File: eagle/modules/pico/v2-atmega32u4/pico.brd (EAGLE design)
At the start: 93.3 x 53.3 mm, 45 parts, among them IC1 MEGA8-AI, IC3 ULN2803A, IC4 ULN2803A, J1 RS232, X1 16MHz

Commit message: Update atmega32u4
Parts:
- added C8: 10u, rcl:SMC_B
- added C9: 100n, SmartPrj:C0603-ROUND
- added F3: MF-MSMF050-2 500mA, rcl:L1812
- added J2: USB MICRO, SmartPrj:CON2_USB_MICRO_B_AT
- added L2: MH2029-300Y, wuerth-elektronik:0805
- added RN3: 22R, resistor-dil:CAY16
- added U1: ATMEGA32U4-XUMU, SmartPrj:QFN44ML7X7
- added Z1, Z2: CG0603MLC-05E, varistor:CT/CN0603
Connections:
- removed net N$4: C1.2, IC1.20
- new net A4: U1.40
- new net A5: U1.41
- new net AVCC: IC1.18
- new net D+: J2.P3, RN3.8, Z1.1
- new net D-: J2.P2, RN3.5, Z2.1
- new net D5*: U1.31
- new net D6*: U1.27
- new net HWB: U1.33
- new net IO10*: U1.30
- new net IO11*: U1.12
- new net IO12: U1.26
- new net IO13*: U1.32
- new net IO8: U1.28
- new net IO9*: U1.29
- new net N$10: C1.2, U1.24, U1.44
- new net N$11: IC1.4, IC1.6
- new net N$12: IC1.3, IC1.5
- new net PAD: U1.EXP
- new net RD+: RN3.1, U1.4
- new net RD-: RN3.4, U1.3
- new net RXLED: U1.8
- new net TXLED: U1.22
- new net UGND: J2.P5, L2.1, U1.5
- new net USBID: J2.P4
- new net UVCC: U1.2
- new net VUSB: C8.+, C9.2, F3.1
- new net XUSB: F3.2, J2.P1
- net 5V: now also U1.14, U1.34, U1.42; no longer IC1.18, IC1.4, IC1.6
- net A0: now also U1.36
- net A1: now also U1.37
- net A2: now also U1.38
- net A3: now also U1.39
- net D14: now also U1.16; no longer IC1.7
- net D15: now also U1.17; no longer IC1.8
- net D4: now also U1.25
- net D7: now also U1.1
- net GND: now also C8.-, C9.1, J2.S1, J2.S2, J2.S3, J2.S4, J2.S5, J2.S6, L2.2, U1.15, U1.23, U1.35, U1.43, Z1.2, Z2.2; no longer IC1.3, IC1.5
- net MISO: now also U1.11; no longer IC1.16
- net MOSI: now also U1.10; no longer IC1.15
- net RESET: now also U1.13; no longer IC1.29
- net RX: now also U1.20; no longer IC1.30
- net SCK: now also U1.9; no longer IC1.17
- net SCL: now also U1.18
- net SDA: now also U1.19; no longer IC1.27
- net TX: now also U1.21; no longer IC1.31

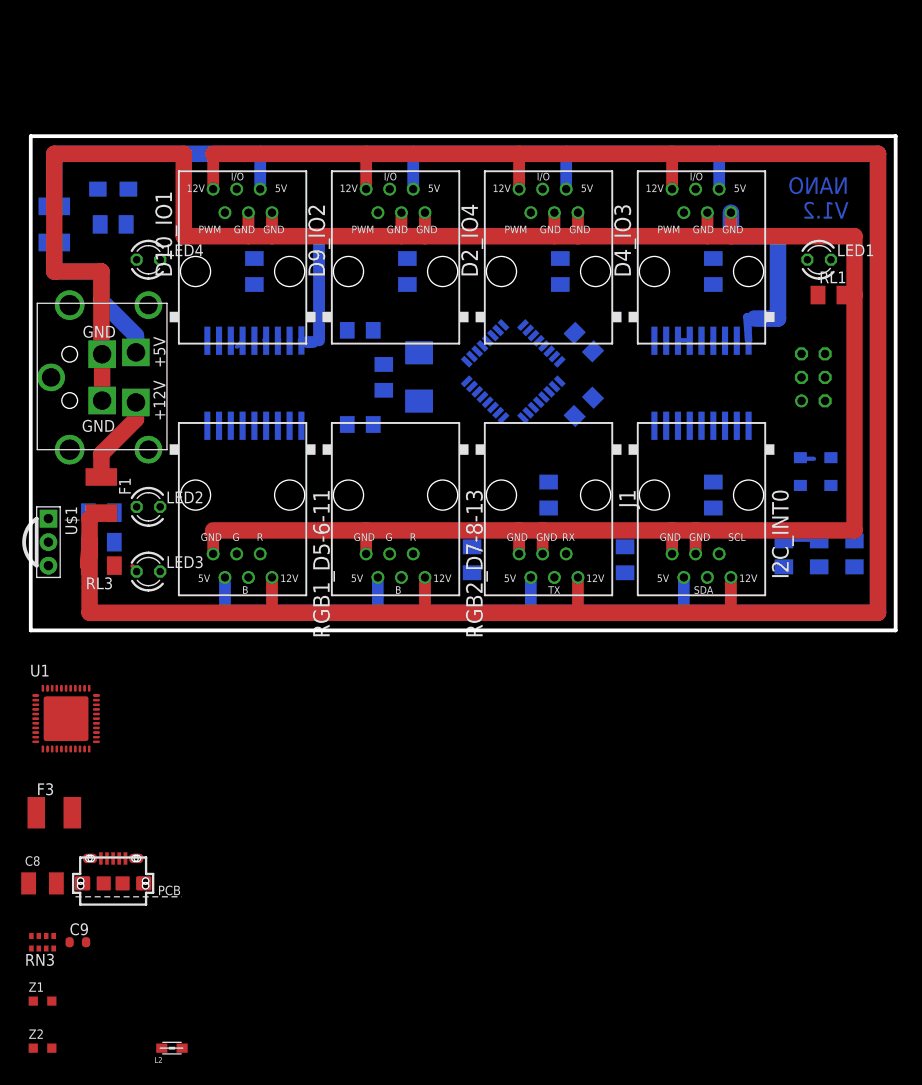
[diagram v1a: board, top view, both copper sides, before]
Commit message: Update library and atmega32u4
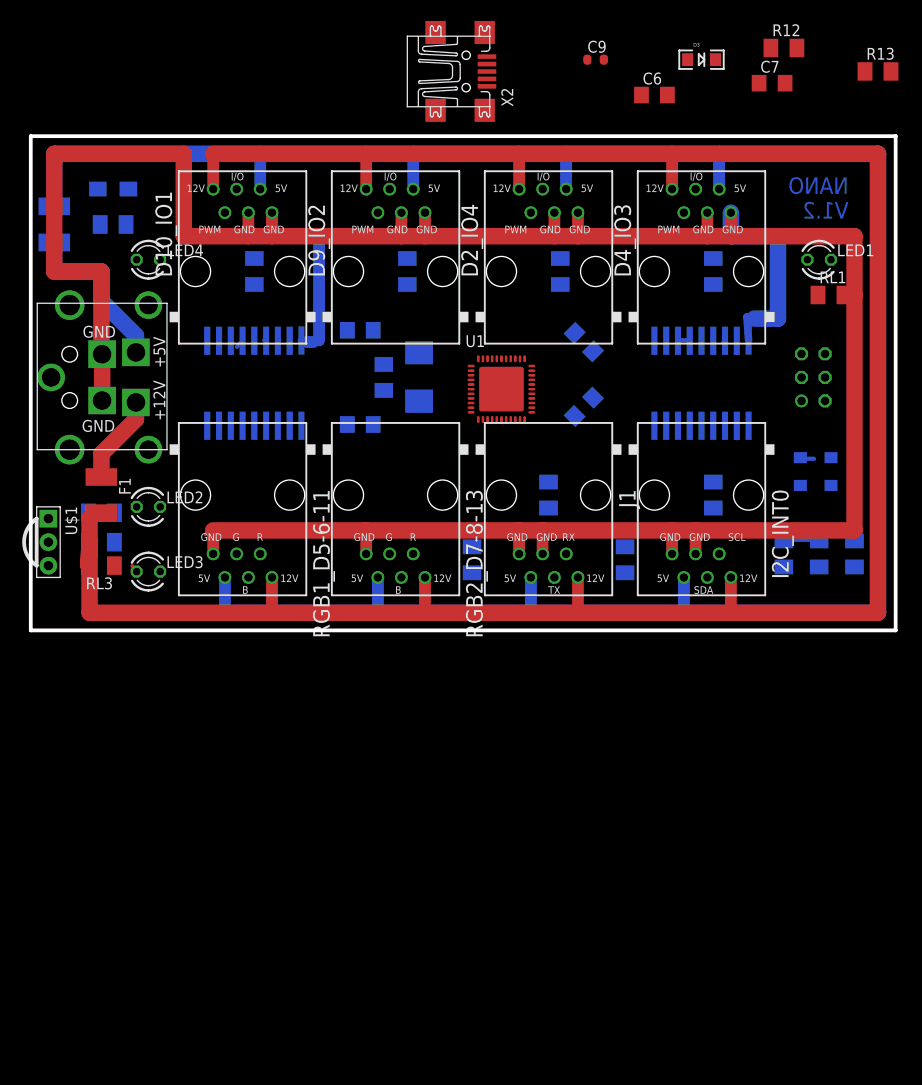
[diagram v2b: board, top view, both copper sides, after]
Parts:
- removed C8: 10u, rcl:SMC_B
- removed F3: MF-MSMF050-2 500mA, rcl:L1812
- removed IC1: MEGA8-AI, atmel:TQFP32-08
- removed J2: USB MICRO, SmartPrj:CON2_USB_MICRO_B_AT
- removed L2: MH2029-300Y, wuerth-elektronik:0805
- removed RN3: 22R, resistor-dil:CAY16
- removed Z1, Z2: CG0603MLC-05E, varistor:CT/CN0603
- added C6: 1uF, resistor:C1206
- added C7: 10uF, resistor:C1206
- added D3: 1N581D1206, lpatiny:LED-1206
- added R12, R13: 22, resistor:M1206
- added X2: MINI-USB-UX60-MB-5ST, con-hirose:UX60-MB-5ST
- moved C9 110.4 mm to (61.0, 61.0)
- moved U1 58.9 mm to (50.8, 25.4)
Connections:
- net IO12 renamed D12
- removed net A0: IC1.23, R0.2, U1.36
- removed net A1: IC1.24, R1B.2, U1.37
- removed net A2: IC1.25, R4.2, U1.38
- removed net A3: IC1.26, R9.2, U1.39
- removed net A4: U1.40
- removed net A5: U1.41
- removed net A6: IC1.19
- removed net A7: IC1.22
- removed net AVCC: IC1.18
- removed net D2: IC1.32, IC3.5
- removed net D3: IC1.1, R11.2
- removed net D5*: U1.31
- removed net D6*: U1.27
- removed net IO10*: U1.30
- removed net IO11*: U1.12
- removed net IO13*: U1.32
- removed net IO8: U1.28
- removed net IO9*: U1.29
- removed net N$11: IC1.4, IC1.6
- removed net N$12: IC1.3, IC1.5
- removed net UGND: J2.P5, L2.1, U1.5
- removed net USBID: J2.P4
- removed net UVCC: U1.2
- removed net XUSB: F3.2, J2.P1
- new net D11: IC3.7, U1.12
- new net D13: IC3.5, U1.32
- new net D18: R4.2, U1.36
- new net D19: R1B.2, U1.37
- new net D20: R0.2, U1.38
- new net D21: IC4.7, IC4.8, R11.2, U1.39
- new net D22: IC3.1, IC3.2, U1.40
- new net D23: IC3.3, IC3.4, U1.41
- new net N$4: C6.1, U1.6
- net 5V: now also C9.2, D3.C, U1.2
- net D+: now also R12.2, X2.3; no longer J2.P3, RN3.8, Z1.1
- net D-: now also R13.2, X2.2; no longer J2.P2, RN3.5, Z2.1
- net D10: now also IC4.5, IC4.6, U1.30; no longer IC1.14, IC3.8
- net D4: now also IC3.8; no longer IC1.2, IC3.6
- net D5: now also U1.31; no longer IC1.9
- net D6: now also IC3.6, U1.27; no longer IC1.10, IC4.3, IC4.4
- net D7: no longer IC1.11, IC4.7, IC4.8
- net D8: now also R9.2, U1.28; no longer IC1.12, IC3.1, IC3.2
- net D9: now also IC4.3, IC4.4, U1.29; no longer IC1.13, IC3.7
- net GND: now also C6.2, C7.1, U1.5, X2.5; no longer C8.-, IC1.21, J2.S1, J2.S2, J2.S3, J2.S4, J2.S5, J2.S6, L2.2, Z1.2, Z2.2
- net MOSI: no longer IC4.5, IC4.6
- net RD+: now also R12.1; no longer RN3.1
- net RD-: now also R13.1; no longer RN3.4
- net SCK: no longer IC3.3, IC3.4
- net SCL: no longer IC1.28
- net VUSB: now also C7.2, D3.A, U1.7, X2.1; no longer C8.+, C9.2, F3.1
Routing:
- net SCK: track 1.36 -> 0.00 mm
- net D23: track 0.00 -> 1.36 mm
- net D6: track 1.10 -> 0.17 mm
- net D9: track 0.21 -> 1.10 mm

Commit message: Update atmega32u8
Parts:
- added LED5: BICOLOR-LED, lpatiny:BICOLOR-3MM
- added RL5, RL6: 1K, resistor:M1206
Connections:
- new net N$11: LED5.3, RL5.2
- new net N$12: LED5.1, RL6.2
- net GND: now also LED5.2
- net RXLED: now also RL5.1
- net TXLED: now also RL6.1
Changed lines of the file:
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@@
 <element name="C6" library="resistor" package="C1206" value="1uF" x="67.31" y="57.15"/>
 <element name="C7" library="resistor" package="C1206" value="10uF" x="80.01" y="58.42"/>
+<element name="LED5" library="lpatiny" package="BICOLOR-3MM" value="BICOLOR-LED" x="2.54" y="-8.89"/>
+<element name="RL5" library="resistor" package="M1206" value="1K" x="2.54" y="-15.24"/>
+<element name="RL6" library="resistor" package="M1206" value="1K" x="2.54" y="-21.59"/>
 </elements>
 <signals>
@@
 <contactref element="C6" pad="2"/>
 <contactref element="C7" pad="1"/>
-<wire x1="80.645" y1="33.02" x2="85.725" y2="29.21" width="0" layer="19" extent="16-16"/>
+<contactref element="LED5" pad="2"/>
+<wire x1="68.71" y1="57.15" x2="78.61" y2="58.42" width="0" layer="19" extent="1-1"/>
+<wire x1="60.071" y1="60.96" x2="68.71" y2="57.15" width="0" layer="19" extent="1-1"/>
+<wire x1="49.24" y1="58.09" x2="60.071" y2="60.96" width="0" layer="19" extent="1-1"/>
+<wire x1="73.025" y1="44.45" x2="68.71" y2="57.15" width="0" layer="19" extent="1-1"/>
 <wire x1="56.515" y1="44.45" x2="56.515" y2="44.2976" width="0" layer="19" extent="1-1"/>
 <wire x1="33.9344" y1="31.496" x2="31.115" y2="30.6578" width="0" layer="19" extent="16-16"/>
@@
 <wire x1="14.0208" y1="5.8928" x2="19.685" y2="7.62" width="0" layer="19" extent="1-1"/>
 <wire x1="7.24" y1="46.99" x2="2.54" y2="50.8" width="0" layer="19" extent="1-16"/>
+<wire x1="85.725" y1="29.21" x2="80.645" y2="33.02" width="0" layer="19" extent="16-16"/>
 <wire x1="34.16" y1="21.59" x2="31.115" y2="30.6578" width="0" layer="19" extent="16-16"/>
+<wire x1="49.8" y1="22.125" x2="52.705" y2="10.16" width="0" layer="19" extent="1-1"/>
+<wire x1="54.075" y1="22.9" x2="49.8" y2="22.125" width="0" layer="19" extent="1-1"/>
+<wire x1="47.525" y1="25.9" x2="49.8" y2="22.125" width="0" layer="19" extent="1-1"/>
+<wire x1="48.8" y1="28.675" x2="47.525" y2="25.9" width="0" layer="19" extent="1-1"/>
+<wire x1="52.8" y1="28.675" x2="48.8" y2="28.675" width="0" layer="19" extent="1-1"/>
+<wire x1="58.700053125" y1="22.50505" x2="54.075" y2="22.9" width="0" layer="19" extent="1-16"/>
 <wire x1="1.905" y1="8.89" x2="13.97" y2="5.715" width="0" layer="19" extent="1-1"/>
-<wire x1="58.700053125" y1="22.50505" x2="55.245" y2="10.16" width="0" layer="19" extent="1-16"/>
-<wire x1="52.8" y1="28.675" x2="13.97" y2="5.715" width="0" layer="19" extent="1-1"/>
-<wire x1="48.8" y1="28.675" x2="52.8" y2="28.675" width="0" layer="19" extent="1-1"/>
-<wire x1="47.525" y1="25.9" x2="48.8" y2="28.675" width="0" layer="19" extent="1-1"/>
-<wire x1="49.8" y1="22.125" x2="47.525" y2="25.9" width="0" layer="19" extent="1-1"/>
-<wire x1="54.075" y1="22.9" x2="49.8" y2="22.125" width="0" layer="19" extent="1-1"/>
-<wire x1="49.24" y1="58.09" x2="42.545" y2="44.45" width="0" layer="19" extent="1-1"/>
-<wire x1="60.071" y1="60.96" x2="49.8" y2="22.125" width="0" layer="19" extent="1-1"/>
-<wire x1="68.71" y1="57.15" x2="60.071" y2="60.96" width="0" layer="19" extent="1-1"/>
-<wire x1="78.61" y1="58.42" x2="68.71" y2="57.15" width="0" layer="19" extent="1-1"/>
+<wire x1="2.54" y1="-8.89" x2="1.905" y2="8.89" width="0" layer="19" extent="1-1"/>
 </signal>
 <signal name="MISO" class="3">
@@
 <signal name="RXLED">
 <contactref element="U1" pad="8"/>
+<contactref element="RL5" pad="1"/>
+<wire x1="1.14" y1="-15.24" x2="47.525" y2="24.4" width="0" layer="19" extent="1-1"/>
 </signal>
 <signal name="HWB">
@@
 <signal name="TXLED">
 <contactref element="U1" pad="22"/>
+<contactref element="RL6" pad="1"/>
+<wire x1="1.14" y1="-21.59" x2="53.3" y2="22.125" width="0" layer="19" extent="1-1"/>
 </signal>
 <signal name="N$10">
@@
 <wire x1="51.3" y1="28.675" x2="57.15" y2="36.7" width="0" layer="19" extent="1-16"/>
 </signal>
+<signal name="N$11">
+<contactref element="RL5" pad="2"/>
+<contactref element="LED5" pad="3"/>
+<wire x1="5.08" y1="-8.89" x2="3.94" y2="-15.24" width="0" layer="19" extent="1-1"/>
+</signal>
+<signal name="N$12">
+<contactref element="LED5" pad="1"/>
+<contactref element="RL6" pad="2"/>
+<wire x1="0" y1="-8.89" x2="3.94" y2="-21.59" width="0" layer="19" extent="1-1"/>
+</signal>
 </signals>

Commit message: Update nano 32u4
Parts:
- removed C9: 100n, SmartPrj:C0603-ROUND
- removed U1: ATMEGA32U4-XUMU, SmartPrj:QFN44ML7X7
- added U2: ATMEGA32U4-XUAU, SmartPrj:TQFP44-PAD
- CON1: device lpatiny:TINYISP -> lpatiny:TC2030-MCP-NL
- LED2: value (none) -> 5V
- LED3: value (none) -> 12V
- LED4: value (none) -> 5V uC
- moved R13 90.4 mm to (12.7, 15.2), turned to 180 degrees
- moved R12 84.6 mm to (12.7, 12.7), turned to 180 degrees
- moved C7 80.1 mm to (13.3, 14.0), flipped to the bottom, turned to 90 degrees
- moved LED1 77.9 mm to (7.62, 47.6), turned to 90 degrees
- moved RL1 69.2 mm to (17.1, 36.8), flipped to the bottom, turned to 90 degrees
- moved D1 67.9 mm to (19.1, 25.4), turned to 180 degrees
- moved D3 65.5 mm to (19.1, 22.9), flipped to the bottom, turned to 180 degrees
- moved RL5 65.3 mm to (20.3, 47.6), turned to 180 degrees
- moved D2 64.1 mm to (19.1, 20.3), turned to 180 degrees
- moved X2 62.5 mm to (5.08, 13.3)
- moved R7 62.0 mm to (27.9, 31.8), turned to 0 degrees
- moved RL6 61.3 mm to (21.0, 36.8), flipped to the bottom, turned to 90 degrees
- moved CON1 57.9 mm to (26.7, 23.5)
- moved LED5 57.7 mm to (14.0, 47.6)
- moved R1 56.9 mm to (33.0, 18.4), turned to 0 degrees
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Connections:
- removed net N$5: IC4.11, IC4.12, RGB2_D7-8-13.R
- new net N$13: IC3.15, IC3.16, RGB2_D7-8-13.R
- net 5V: now also U2.14, U2.2, U2.34, U2.42; no longer C9.2, U1.14, U1.2, U1.34, U1.42
- net D10: now also U2.30; no longer U1.30
- net D11: now also U2.12; no longer U1.12
- net D12: now also U2.26; no longer U1.26
- net D13: now also U2.32; no longer U1.32
- net D14: now also U2.16; no longer U1.16
- net D15: now also U2.17; no longer U1.17
- net D18: now also U2.36; no longer U1.36
- net D19: now also U2.37; no longer U1.37
- net D20: now also U2.38; no longer U1.38
- net D21: now also U2.39; no longer U1.39
- net D22: now also U2.40; no longer U1.40
- net D23: now also U2.41; no longer U1.41
- net D4: now also U2.25; no longer U1.25
- net D5: now also U2.31; no longer U1.31
- net D6: now also U2.27; no longer U1.27
- net D7: now also U2.1; no longer U1.1
- net D8: now also U2.28; no longer U1.28
- net D9: now also U2.29; no longer U1.29
- net GND: now also LED1.K, U2.15, U2.23, U2.35, U2.43, U2.5; no longer C9.1, RL1.2, U1.15, U1.23, U1.35, U1.43, U1.5
- net HWB: now also U2.33; no longer U1.33
- net ISP+5V: now also CON1.5V; no longer CON1.VCC
- net MISO: now also U2.11; no longer U1.11
- net MOSI: now also U2.10; no longer U1.10
- net N$1: now also IC4.17, IC4.18; no longer IC4.13, IC4.14
- net N$10: now also U2.24, U2.44; no longer U1.24, U1.44
- net N$3: now also LED1.A, RL1.2; no longer LED1.K, RL1.1
- net N$4: now also U2.6; no longer U1.6
- net N$57: now also IC4.11, IC4.12; no longer IC3.15, IC3.16
- net N$68: now also IC4.13, IC4.14; no longer IC4.17, IC4.18
- net PAD: now also U2.P$1; no longer U1.EXP
- net RD+: now also U2.4; no longer U1.4
- net RD-: now also U2.3; no longer U1.3
- net RESET: now also U2.13; no longer U1.13
- net RX: now also U2.20; no longer U1.20
- net RXLED: now also U2.8; no longer U1.8
- net SCK: now also RL1.1, U2.9; no longer LED1.A, U1.9
- net SCL: now also U2.18; no longer U1.18
- net SDA: now also U2.19; no longer U1.19
- net TX: now also U2.21; no longer U1.21
- net TXLED: now also U2.22; no longer U1.22
- net VUSB: now also U2.7; no longer U1.7
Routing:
- net +12V: track 253.4 -> 216.8 mm, vias 0 -> 1
- net N$8: track 9.60 -> 32.1 mm
- net +5V: track 246.8 -> 234.9 mm
- net GND: track 311.3 -> 300.4 mm
- net SCL: track 3.95 -> 0.00 mm
- net D23: track 1.36 -> 0.00 mm
- net N$51: track 1.33 -> 0.00 mm
- net D9: track 1.10 -> 0.00 mm
- net N$75: track 0.89 -> 0.00 mm
- net N$6: track 19.1 -> 19.8 mm
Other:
- board text added: "NANO V2.0"
- board text removed: "NANO V1.2"

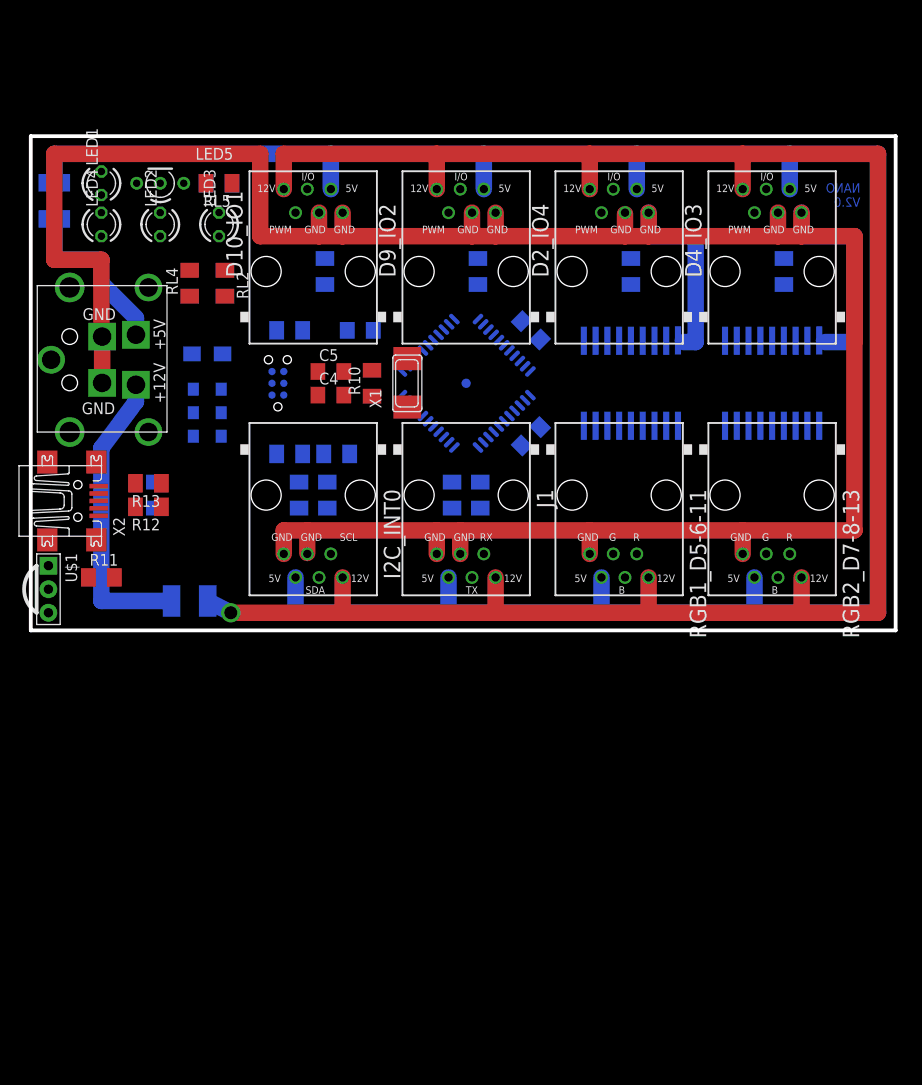
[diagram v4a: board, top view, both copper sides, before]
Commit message: Update I2C addresses
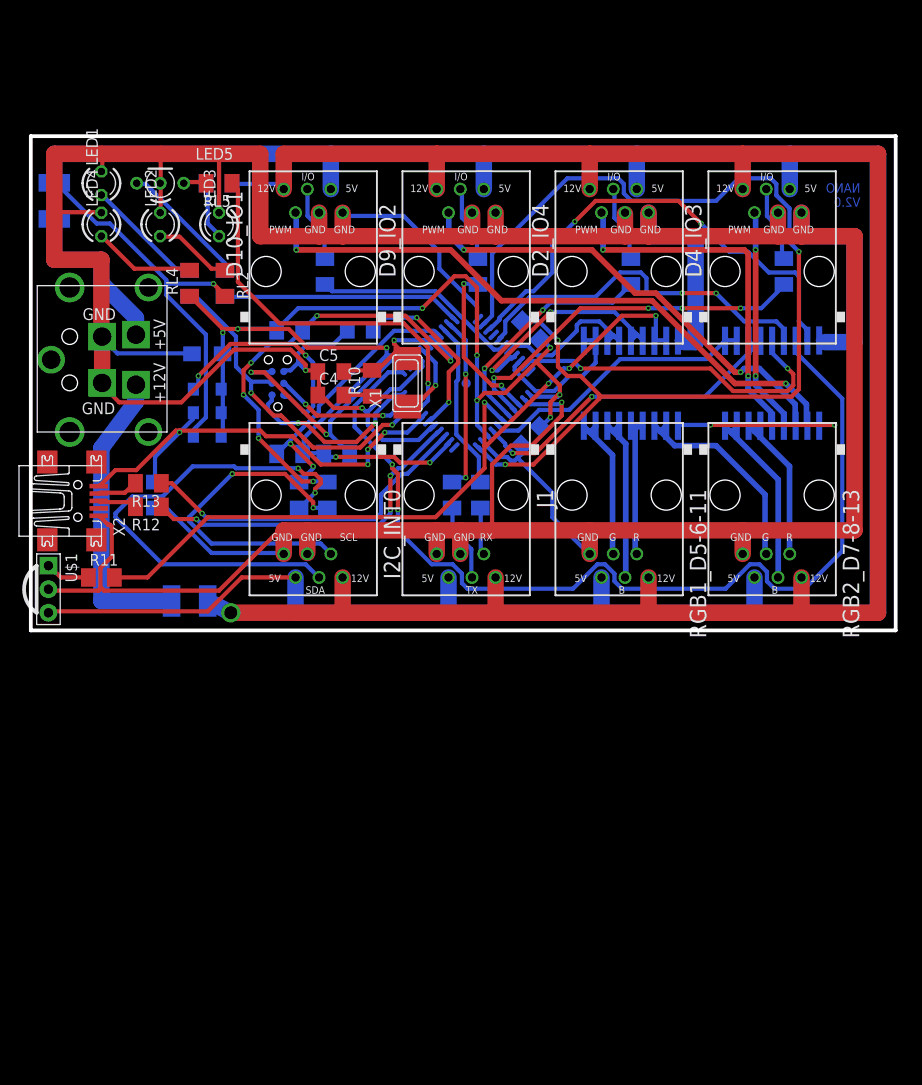
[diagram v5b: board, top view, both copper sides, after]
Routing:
- net GND: track 300.4 -> 514.4 mm, vias 0 -> 3
- net 5V: track 0.00 -> 141.1 mm, vias 0 -> 11
- net N$10: track 0.00 -> 120.5 mm, vias 0 -> 3
- net D11: track 0.00 -> 105.1 mm, vias 0 -> 2
- net D21: track 0.00 -> 83.3 mm, vias 0 -> 4
- net +5V: track 234.9 -> 305.8 mm, vias 0 -> 1
- net N$51: track 0.00 -> 68.4 mm, vias 0 -> 2
- net D2B4: track 0.00 -> 54.0 mm, vias 0 -> 2
- net D4: track 0.00 -> 51.9 mm, vias 0 -> 2
- net VUSB: track 0.00 -> 51.6 mm, vias 0 -> 4
- net N$22: track 0.00 -> 50.0 mm, vias 0 -> 2
- net SCL: track 0.00 -> 47.2 mm, vias 0 -> 6
- net RXLED: track 0.00 -> 41.6 mm, vias 0 -> 1
- net D19: track 0.00 -> 40.0 mm, vias 0 -> 4
- net N$60: track 0.00 -> 39.6 mm, vias 0 -> 2
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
